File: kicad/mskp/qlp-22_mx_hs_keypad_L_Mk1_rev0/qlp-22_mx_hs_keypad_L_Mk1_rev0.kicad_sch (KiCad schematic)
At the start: 23 parts, among them J1 Conn_01x12_Pin, SW1 Switch, SW10 Switch, SW11 Switch, SW12 Switch, SW13 Switch, SW4 Switch, SW5 Switch, SW6 Switch, SW7 Switch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

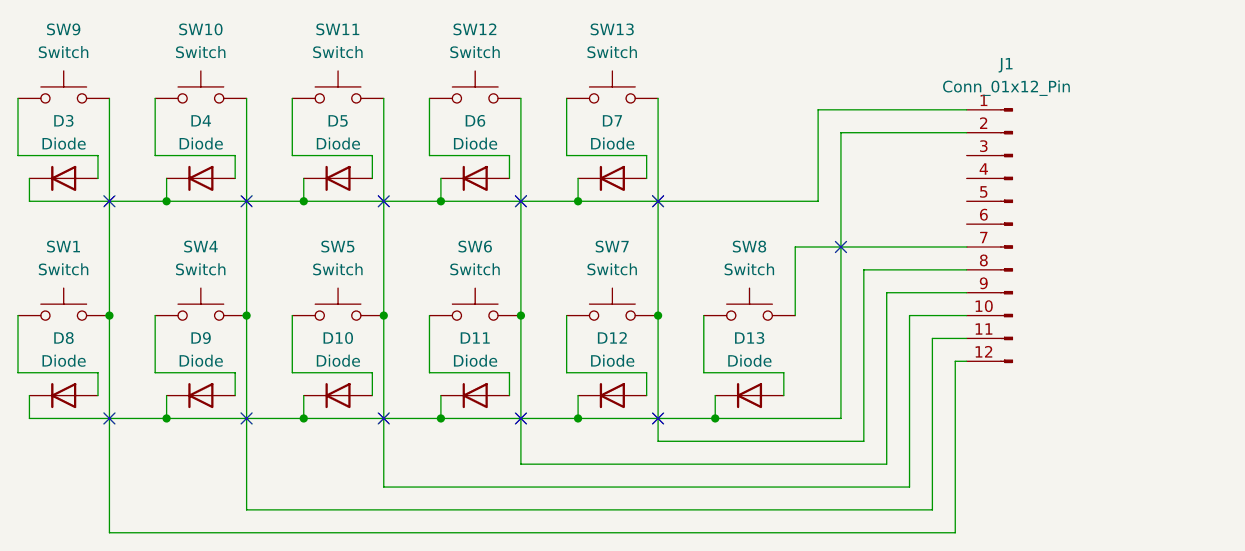
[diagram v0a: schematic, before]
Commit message: Removes the mksp_Mk1_rev0 project in favor of board-specific projects
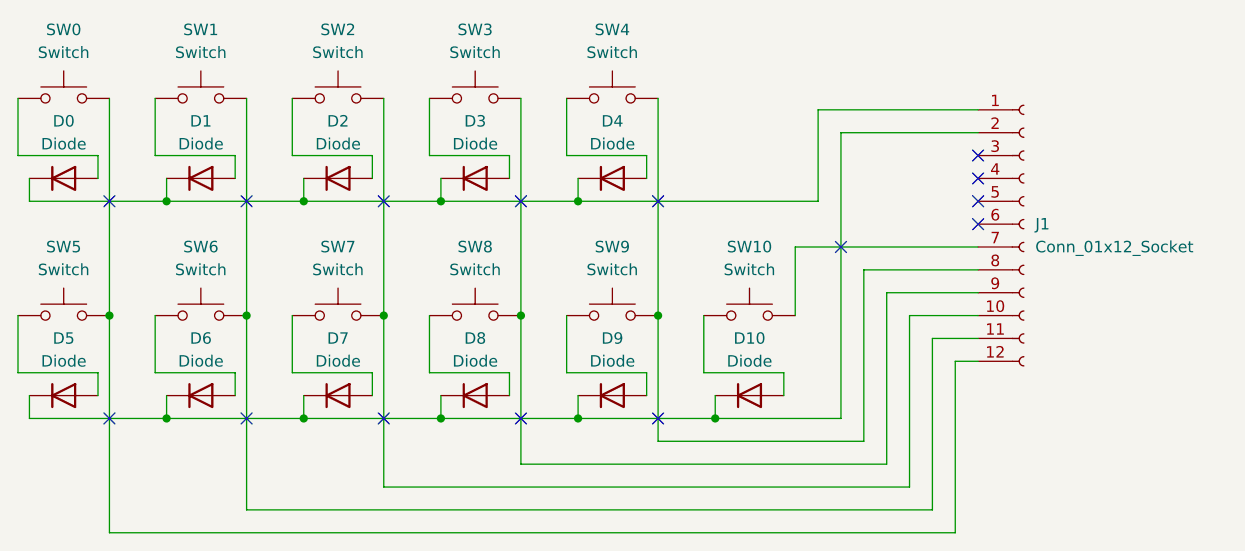
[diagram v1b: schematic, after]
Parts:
- removed J1: Conn_01x12_Pin, symbol Connector:Conn_01x12_Pin
- added J1: Conn_01x12_Socket, Connector_JST:JST_GH_SM12B-GHS-TB_1x12-1MP_P1.25mm_Horizontal, symbol Connector:Conn_01x12_Socket
- D0: renamed from D3; footprint (none) -> ScottoKeebs_Components:Diode_DO-35
- D1: renamed from D4; footprint (none) -> ScottoKeebs_Components:Diode_DO-35
- D10: renamed from D13; footprint (none) -> ScottoKeebs_Components:Diode_DO-35
- D2: renamed from D5; footprint (none) -> ScottoKeebs_Components:Diode_DO-35
- D3: renamed from D6; footprint (none) -> ScottoKeebs_Components:Diode_DO-35
- D4: renamed from D7; footprint (none) -> ScottoKeebs_Components:Diode_DO-35
- D5: renamed from D8; footprint (none) -> ScottoKeebs_Components:Diode_DO-35
- D6: renamed from D9; footprint (none) -> ScottoKeebs_Components:Diode_DO-35
- D7: renamed from D10; footprint (none) -> ScottoKeebs_Components:Diode_DO-35
- D8: renamed from D11; footprint (none) -> ScottoKeebs_Components:Diode_DO-35
- D9: renamed from D12; footprint (none) -> ScottoKeebs_Components:Diode_DO-35
- SW0: renamed from SW9; footprint (none) -> ScottoKeebs_Hotswap:Hotswap_MX_1.00u
- SW1: renamed from SW10; footprint (none) -> ScottoKeebs_Hotswap:Hotswap_MX_1.00u
- SW10: renamed from SW8; footprint (none) -> ScottoKeebs_Hotswap:Hotswap_MX_1.00u
- SW2: renamed from SW11; footprint (none) -> ScottoKeebs_Hotswap:Hotswap_MX_1.00u
- SW3: renamed from SW12; footprint (none) -> ScottoKeebs_Hotswap:Hotswap_MX_1.00u
- SW4: renamed from SW13; footprint (none) -> ScottoKeebs_Hotswap:Hotswap_MX_1.00u
- SW5: renamed from SW1; footprint (none) -> ScottoKeebs_Hotswap:Hotswap_MX_1.00u
- SW6: renamed from SW4; footprint (none) -> ScottoKeebs_Hotswap:Hotswap_MX_1.00u
- SW7: renamed from SW5; footprint (none) -> ScottoKeebs_Hotswap:Hotswap_MX_1.00u
- SW8: renamed from SW6; footprint (none) -> ScottoKeebs_Hotswap:Hotswap_MX_1.00u
- SW9: renamed from SW7; footprint (none) -> ScottoKeebs_Hotswap:Hotswap_MX_1.00u
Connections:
- net at D0.1 (K), D1.1 (K), D2.1 (K)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: now also J1.1 (Pin_1)
- net at SW2.2, SW7.2: now also J1.10 (Pin_10)
- net at SW1.2, SW6.2: now also J1.11 (Pin_11)
- net at D10.1 (K), D5.1 (K), D6.1 (K)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: now also J1.2 (Pin_2)
- net at SW3.2, SW8.2: now also J1.9 (Pin_9)
- net at SW4.2, SW9.2: now also J1.8 (Pin_8)
- net at SW10.2: now also J1.7 (Pin_7)
- net at SW0.2, SW5.2: now also J1.12 (Pin_12)
- no-connect marks 11 -> 15
